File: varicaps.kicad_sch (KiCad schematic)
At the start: 8 parts, among them U701 16.5pF~33pF, U702 16.5pF~33pF, U703 16.5pF~33pF, U704 16.5pF~33pF, U705 16.5pF~33pF, U706 16.5pF~33pF

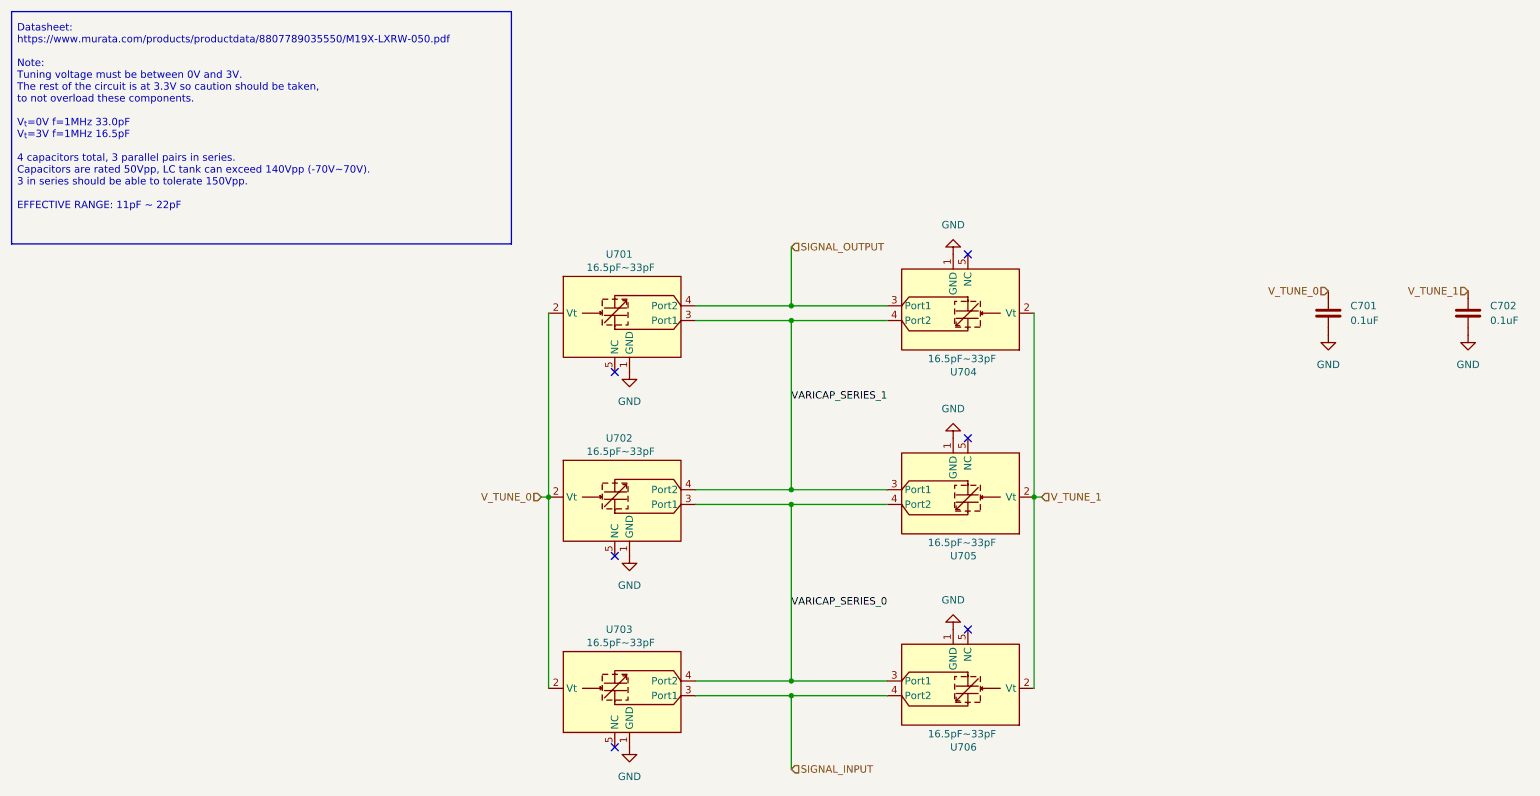
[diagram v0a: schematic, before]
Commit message: Starting work on OmniStimDriverBoard design
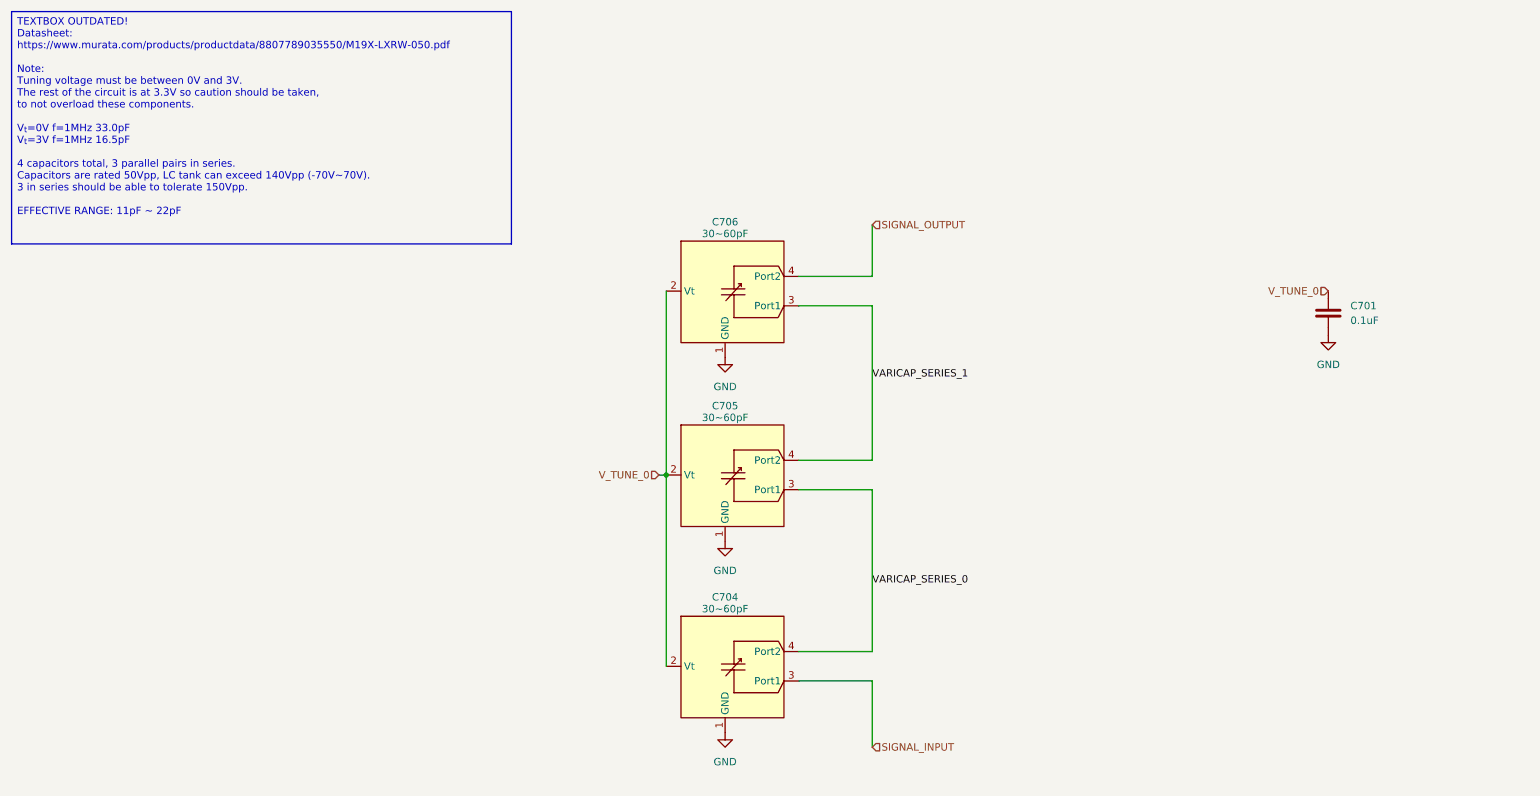
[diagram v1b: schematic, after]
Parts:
- removed C702: 0.1uF, easyeda2kicad:C0402, symbol easyeda2kicad:GRM155R71A104KA01J
- removed U701, U702, U703, U704, U705, U706: 16.5pF~33pF, easyeda2kicad:DFN-4_L1.3-W0.9-P0.50-BR, symbol easyeda2kicad:LXRW19V330-050
- added C704, C705, C706: 30~60pF, easyeda2kicad:X2SON-4_L0.6-W0.6-P0.40-BL, symbol easyeda2kicad:LXRW0YV600-054
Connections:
- net GND: now also C704.1 (GND), C705.1 (GND), C706.1 (GND)
- net SIGNAL_INPUT: now also C704.3 (Port1)
- net SIGNAL_OUTPUT: now also C706.4 (Port2)
- net VARICAP_SERIES_0: now also C704.4 (Port2), C705.3 (Port1)
- net VARICAP_SERIES_1: now also C705.4 (Port2), C706.3 (Port1)
- net V_TUNE_0: now also C704.2 (Vt), C705.2 (Vt), C706.2 (Vt)
- no-connect marks 6 -> 0
